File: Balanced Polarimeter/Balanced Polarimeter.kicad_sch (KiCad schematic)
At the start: 4 parts, among them Q1 MMPQ3904, Q2 MMPQ3904

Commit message: Added SS and TA
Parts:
- added R3, R4, R5, R6, R7, R8: 20k, symbol Device:R
- added U1, U2, U3: ADA4898-1YRDZ, Package_SO:SOIC-8-1EP_3.9x4.9mm_P1.27mm_EP2.29x3mm, symbol Amplifier_Operational:ADA4898-1YRDZ
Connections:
- net -5V: now also U1.4 (V-), U2.4 (V-), U3.4 (V-)
- net GND: now also R6.1
- net at Q2.5 (COLLECTOR_#3_1), Q2.6 (COLLECTOR_#3_2): now also U2.3 (+)
- net at Q1.5 (COLLECTOR_#3_1), Q1.6 (COLLECTOR_#3_2): now also U1.3 (+)
- net 5V: no longer names the net of Q2.3 (COLLECTOR_#2_1), Q2.4 (COLLECTOR_#2_2)
- net 5V: no longer Q1.3 (COLLECTOR_#2_1), Q1.4 (COLLECTOR_#2_2)
- new net: R4.1, R7.1, U2.6
- new net: R7.2, R8.2, U3.2 (-)
- new net: R5.1, R6.2, U3.3 (+)
- new net: R3.1, R5.2, U1.6
- new net: R4.2, U2.2 (-)
- new net: R8.1, U3.6
- new net: Q1.3 (COLLECTOR_#2_1), Q1.4 (COLLECTOR_#2_2)
- new net: R3.2, U1.2 (-)
- new net +5V: U1.7 (V+), U2.7 (V+), U3.7 (V+)
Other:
- moved on the sheet: Q1, R1

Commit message: Updates
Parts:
- added D1, D2: S5971, Package_TO_SOT_THT:TO-18-3, symbol Sensor_Optical:S5971
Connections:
- net +5V: now also D1.3 (A), D2.3 (A)
- net GND: now also D1.2 (C), D2.2 (C)
- net at Q2.3 (COLLECTOR_#2_1), Q2.4 (COLLECTOR_#2_2): now also D1.1 (K)
- net V_out: now reaches R8.1, U3.6
- net at Q1.3 (COLLECTOR_#2_1), Q1.4 (COLLECTOR_#2_2): now also D2.1 (K)
- no-connect marks 0 -> 6

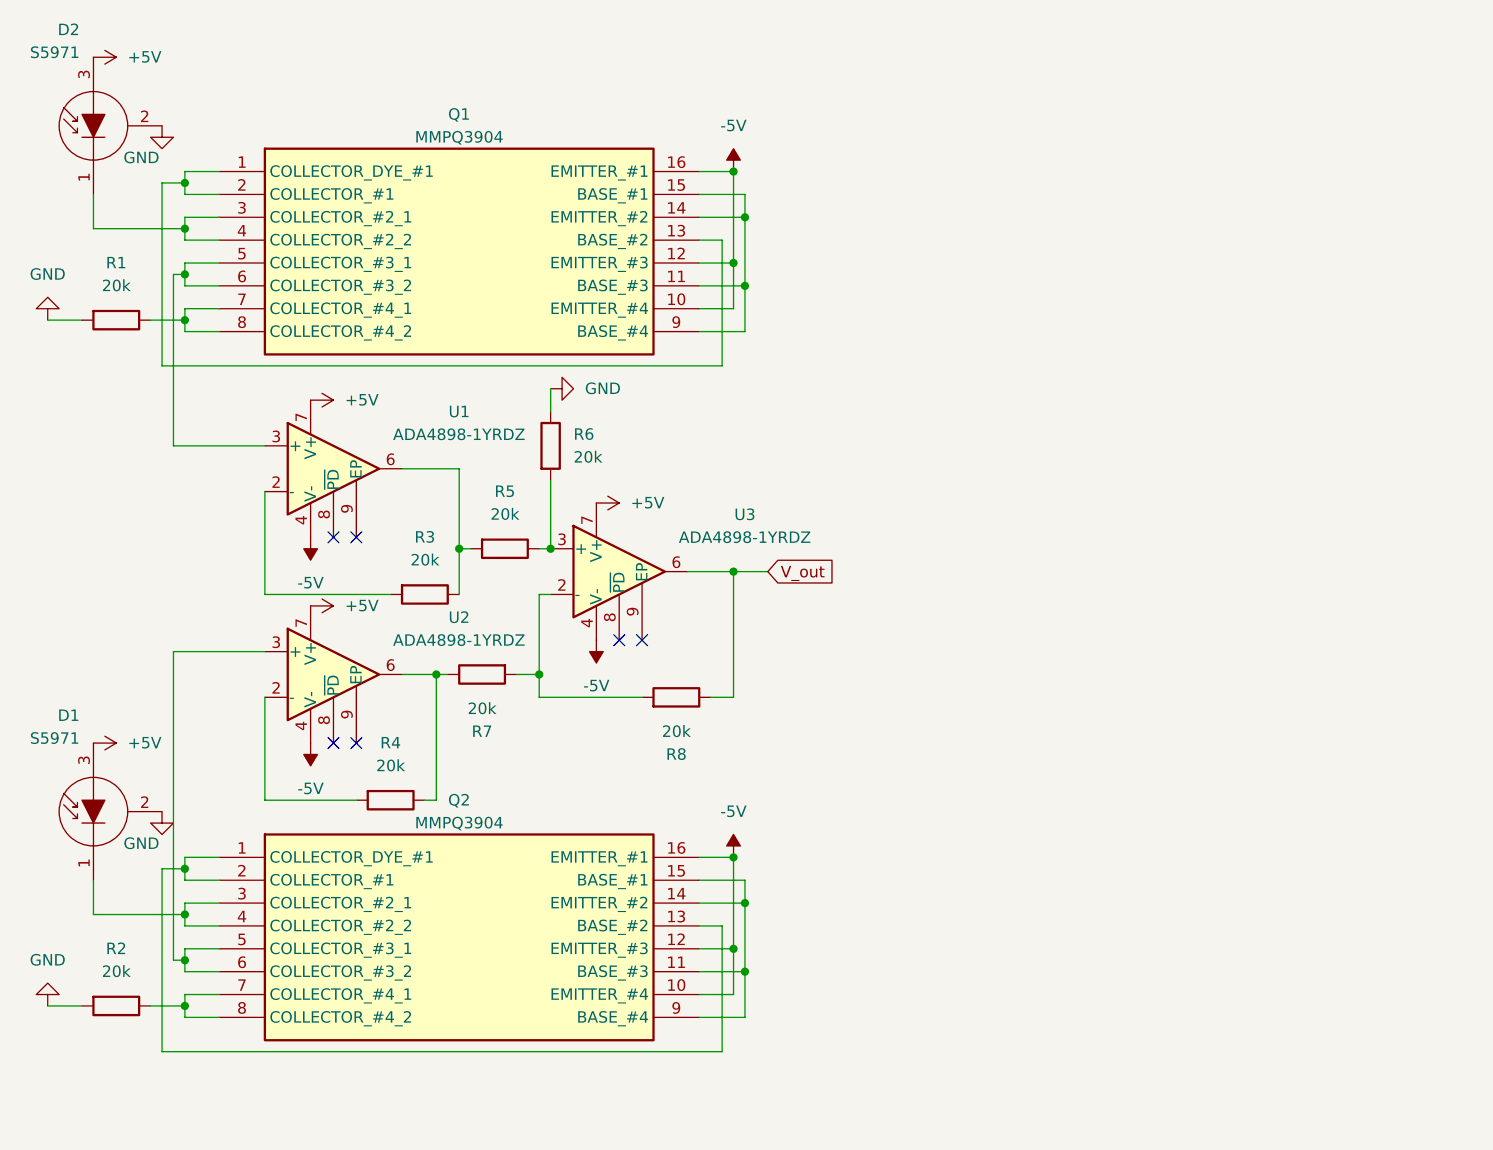
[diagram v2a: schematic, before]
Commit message: Next revision
Rewired all powers to a single node and swapped the op amp for an op27
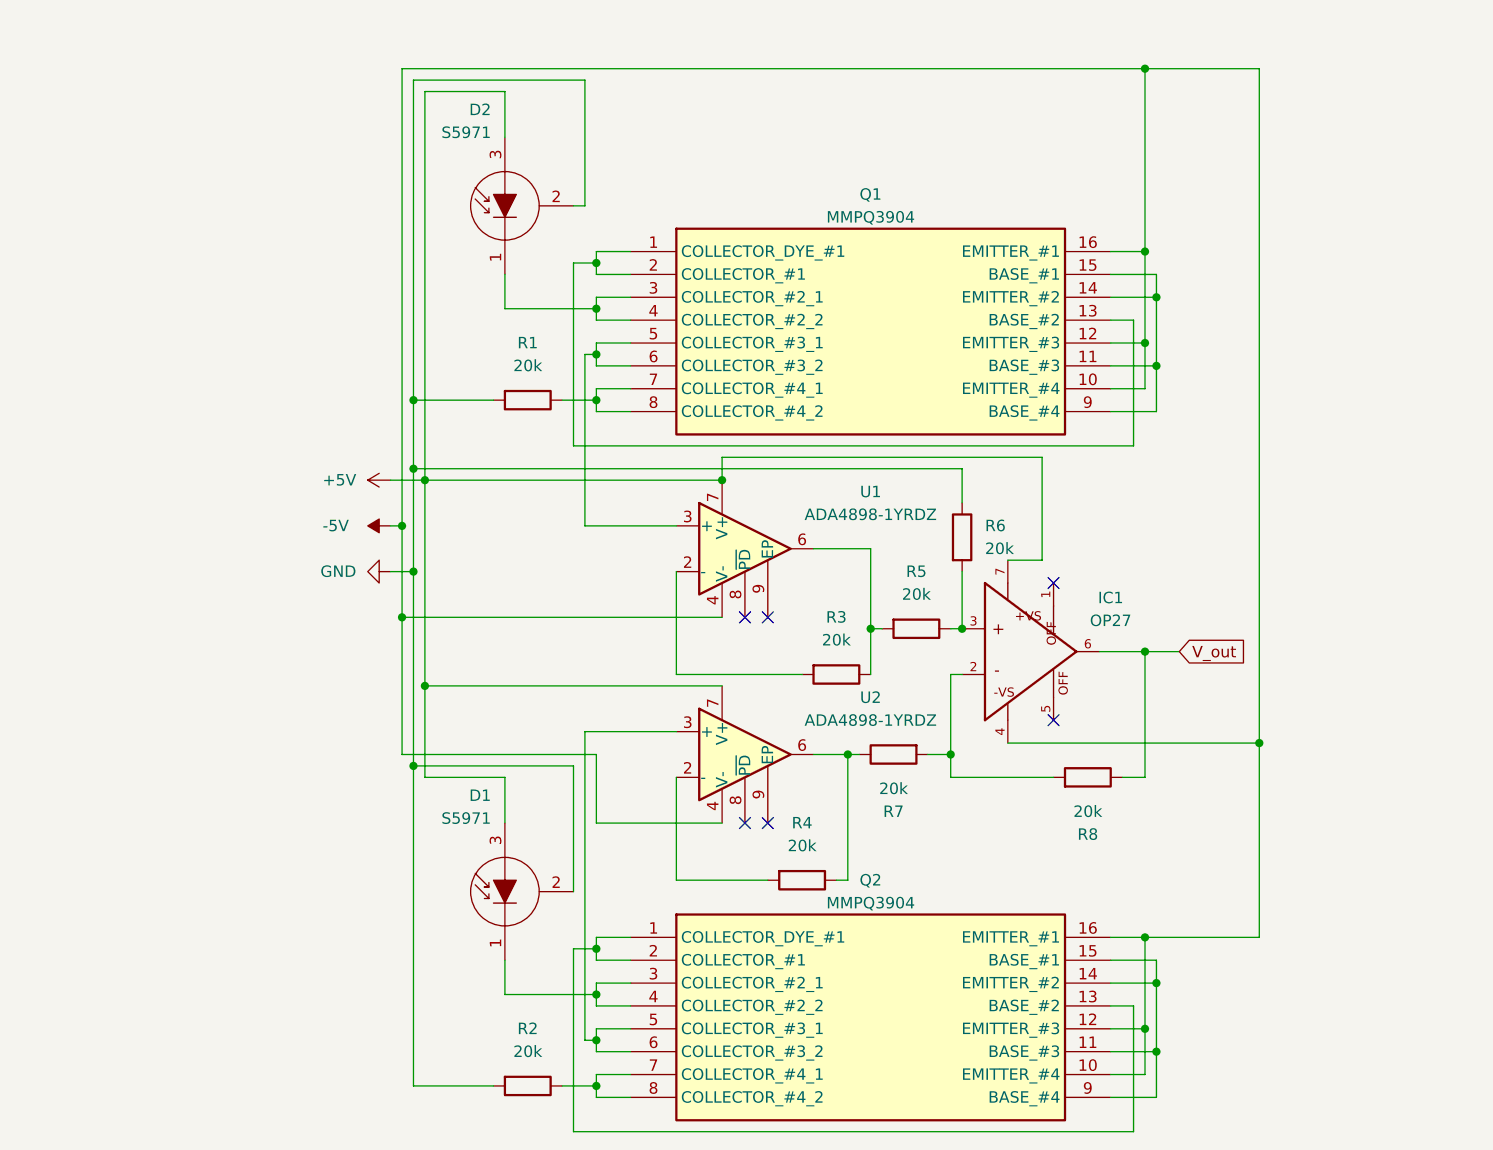
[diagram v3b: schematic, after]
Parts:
- removed U3: ADA4898-1YRDZ, Package_SO:SOIC-8-1EP_3.9x4.9mm_P1.27mm_EP2.29x3mm, symbol Amplifier_Operational:ADA4898-1YRDZ
- added IC1: OP27, OP27:DIL08, symbol OP27:OP27
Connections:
- net +5V: now also IC1.7
- net -5V: now also IC1.4
- net V_out: now also IC1.6
- net at R7.2, R8.2: now also IC1.2
- net at R5.1, R6.2: now also IC1.3
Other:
- moved on the sheet: D1, D2, Q1, Q2, R1, R2, R3, R4, R5, R6, R7, R8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
